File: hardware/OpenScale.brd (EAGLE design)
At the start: 54.6 x 40.6 mm, 58 parts, among them U1 HX711, U3 TMP102, U4 ATMEGA328P_TQFP, U5 MIC52055-5V, U6 FT231X, Y2 16MHZ

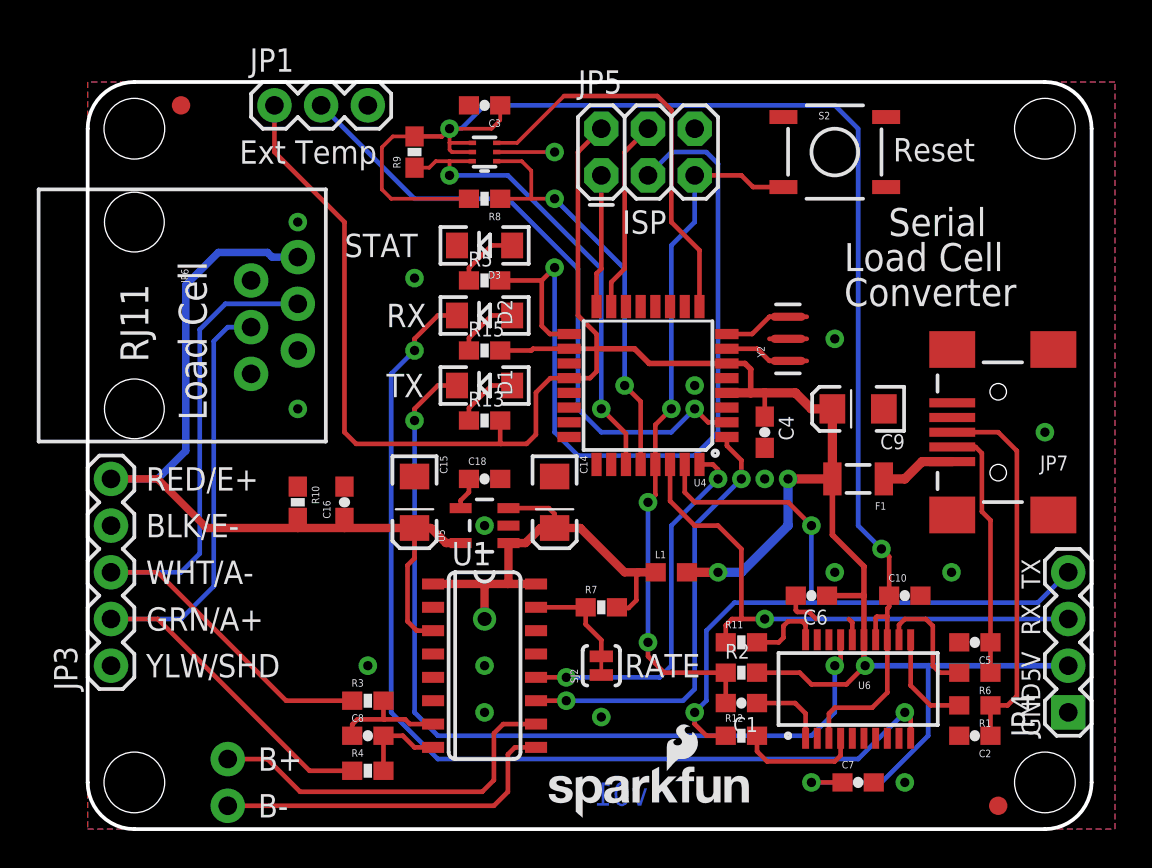
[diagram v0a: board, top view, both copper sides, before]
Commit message: Lots of changes. v02 ready for proto.
Changed to RJ45, FTDI connection, MOSFETs to temp sensor, silk, shutdown
from temp sensor to ATmega.
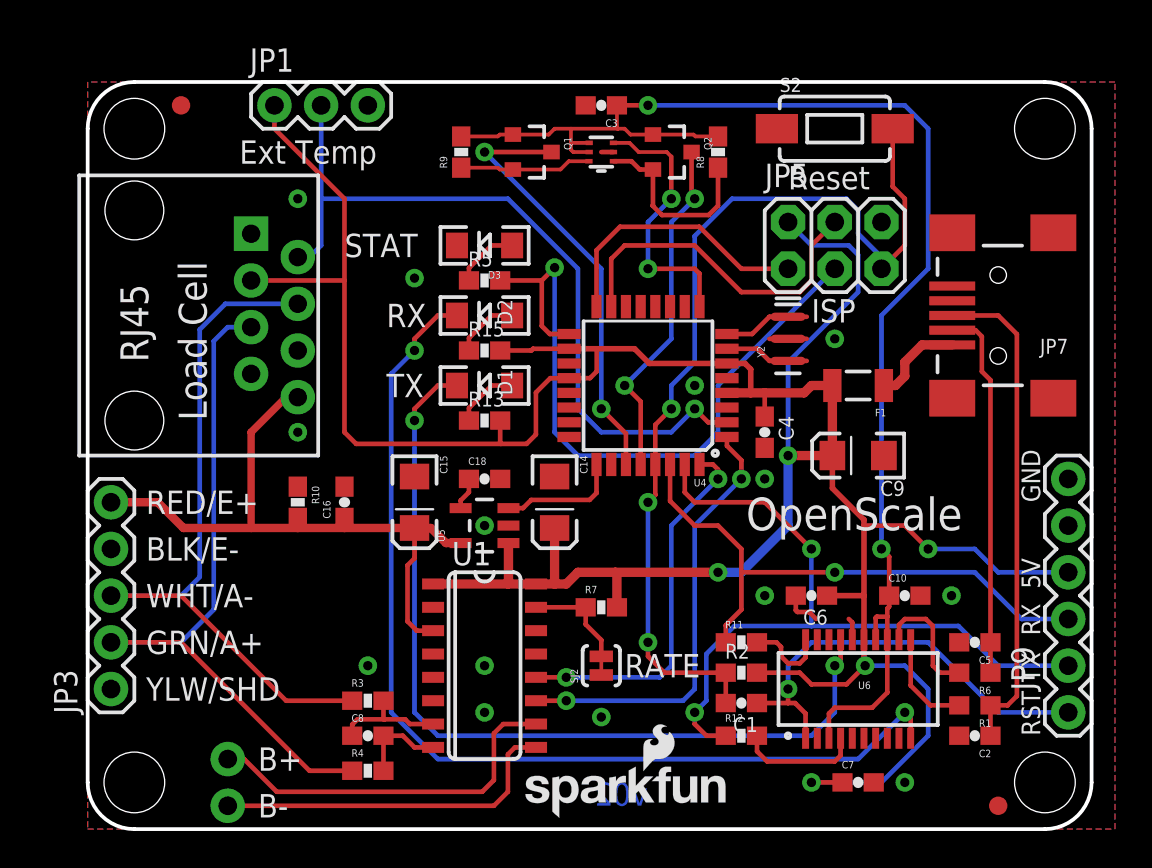
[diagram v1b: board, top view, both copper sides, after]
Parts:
- removed JP4: (no value), SparkFun-Connectors:1X04
- removed L1: 30Ohm 1.8A, SparkFun-Passives:0603
- added JP9: FTDI_BASIC, SparkFun-Connectors:FTDI_BASIC
- added Q1, Q2: 200mA/50V, SparkFun-DiscreteSemi:SOT23-3
- JP6: value RJ11 -> RJ45; device SparkFun-Connectors:RJ11-6 -> SparkFun-Connectors:RJ45-8
- R5: value 330 -> 1K
- S2: device SparkFun-Electromechanical:TACTILE-SWITCH-SMD -> SparkFun-Electromechanical:TACTILE-SWITCH-1101NE
- moved R8 13.0 mm to (34.3, 36.8), turned to 90 degrees
- moved JP5 11.4 mm to (38.1, 30.5)
- moved C3 6.35 mm to (27.9, 39.4)
- moved JP7 6.35 mm to (49.5, 27.9)
- moved U3 6.35 mm to (27.9, 36.8)
- moved F1 5.08 mm to (41.9, 24.1)
- moved C9 2.54 mm to (41.9, 20.3)
- moved R9 2.54 mm to (20.3, 36.8)
- moved LOGO1 1.27 mm to (23.4, 0.51)
- moved S2 1.27 mm to (40.6, 38.1)
- moved JP3 1.27 mm to (1.27, 7.62)
- moved LOGO4 0.89 mm to (33.1, 17.8)
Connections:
- removed net VCC: C14.A, L1.1, R7.2, U1.1, U1.16, U5.1, U5.3
- new net AMP_EN: U4.25, U5.3
- new net LV_SCL: Q2.2, R8.1, U3.1
- new net LV_SDA: Q1.2, R9.1, U3.6
- net 3.3V: now also Q1.1, Q2.1
- net 5V: now also C14.A, JP6.3, JP9.VCC, R7.2, U1.1, U1.16, U5.1; no longer JP4.2, L1.2
- net A+: now also JP6.5; no longer JP6.4
- net A-: now also JP6.4; no longer JP6.3
- net AVDD: now also JP6.8; no longer JP6.1
- net DTR: now also JP9.DTR
- net GND: now also JP6.1, JP6.6, JP6.7, JP9.GND; no longer JP4.1, JP6.2, JP6.5
- net RST: now also S2.2; no longer S2.3
- net RXD: now also JP9.TXO; no longer JP4.3
- net SCL: now also Q2.3; no longer R8.1, U3.1
- net SDA: now also Q1.3; no longer R9.1, U3.6
- net TEMP_DAT: now also JP6.2
- net TXD: now also JP9.RXI; no longer JP4.4
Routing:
- net 5V: track 133.4 -> 170.1 mm, vias 4 -> 5
- net VCC: track 25.3 -> 0.00 mm, vias 1 -> 0
- net DTR: track 4.23 -> 23.6 mm, vias 0 -> 1
- net RST: track 38.6 -> 52.3 mm
- net AVDD: track 49.1 -> 36.4 mm
- net LV_SCL: track 0.00 -> 10.4 mm
- net D11: track 10.5 -> 18.8 mm
- net D12: track 7.25 -> 15.0 mm
- net D13: track 45.5 -> 37.8 mm
- net ALERT: track 22.2 -> 14.8 mm, vias 0 -> 2
- net LV_SDA: track 0.00 -> 7.18 mm
- net TEMP_DAT: track 34.7 -> 41.8 mm
- net AMP_EN: track 0.00 -> 6.69 mm
- net N$7: track 20.6 -> 26.9 mm
- net N$4: track 13.9 -> 20.2 mm
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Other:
- board text added: "BLK"
- board text added: "FTDI"
- board text added: "GRN"
- board text added: "OpenScale"
- board text added: "RJ45"
- board text added: "RST"
- board text removed: "Converter"
- board text removed: "RJ11"
- board text removed: "Serial"

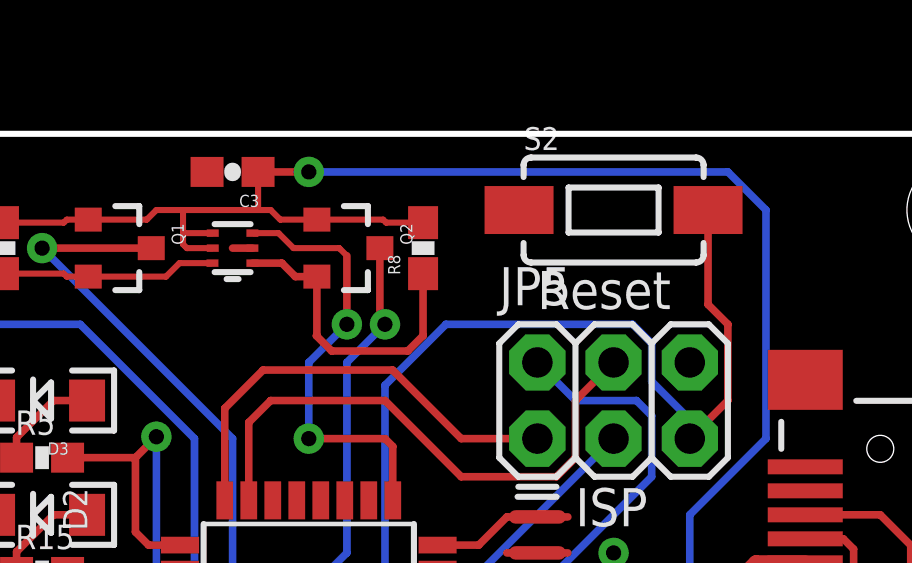
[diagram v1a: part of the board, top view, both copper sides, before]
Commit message: Silk fix. Dim fix. Reroute traces to TMP102.
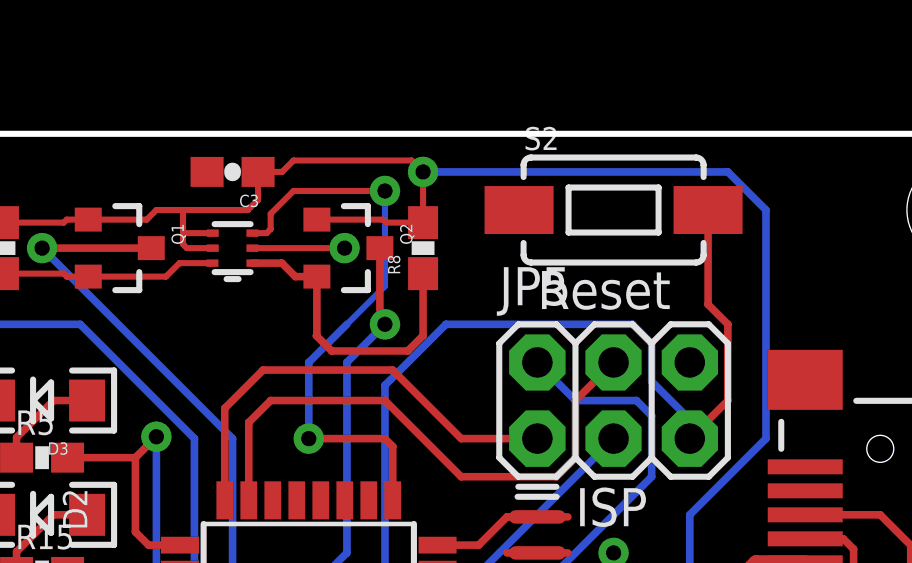
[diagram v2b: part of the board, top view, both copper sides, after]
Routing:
- net ALERT: track 14.8 -> 19.3 mm
- net GND: track 3.97 -> 6.38 mm, vias 14 -> 15
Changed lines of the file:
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@@
 <layer number="39" name="tKeepout" color="4" fill="11" visible="no" active="yes"/>
 <layer number="40" name="bKeepout" color="1" fill="11" visible="no" active="yes"/>
-<layer number="41" name="tRestrict" color="4" fill="10" visible="no" active="yes"/>
+<layer number="41" name="tRestrict" color="4" fill="10" visible="yes" active="yes"/>
 <layer number="42" name="bRestrict" color="1" fill="10" visible="no" active="yes"/>
 <layer number="43" name="vRestrict" color="2" fill="10" visible="no" active="yes"/>
@@
 <text x="3.175" y="17.145" size="1.27" layer="21" font="vector" ratio="15">RED/E+</text>
 <text x="35.56" y="15.113" size="2.032" layer="22" font="vector" ratio="15" rot="MR0">OpenScale</text>
-<text x="15.24" y="30.48" size="1.27" layer="22" font="vector" ratio="15" rot="MR0">E+</text>
-<text x="15.24" y="27.94" size="1.27" layer="22" font="vector" ratio="15" rot="MR0">A-</text>
-<text x="16.129" y="25.4" size="1.27" layer="22" font="vector" ratio="15" rot="MR0">SHD</text>
-<text x="7.0485" y="24.1935" size="1.27" layer="22" font="vector" ratio="15" rot="MR0">B+</text>
+<text x="12.7" y="24.13" size="1.27" layer="22" font="vector" ratio="15" rot="MR180">E+</text>
+<text x="12.7" y="29.21" size="1.27" layer="22" font="vector" ratio="15" rot="MR180">A-</text>
+<text x="12.7" y="26.67" size="1.27" layer="22" font="vector" ratio="15" rot="MR180">SHD</text>
 <text x="7.0485" y="26.6065" size="1.27" layer="22" font="vector" ratio="15" rot="MR0">A+</text>
-<text x="7.0485" y="29.1465" size="1.27" layer="22" font="vector" ratio="15" rot="MR0">E-</text>
+<text x="7.0485" y="24.0665" size="1.27" layer="22" font="vector" ratio="15" rot="MR0">E-</text>
 <text x="3.302" y="25.4" size="1.524" layer="21" font="vector" ratio="15" rot="R90">RJ45</text>
 <text x="6.477" y="22.225" size="1.524" layer="21" font="vector" ratio="15" rot="R90">Load Cell</text>
@@
 <dimension x1="0" y1="40.64" x2="54.61" y2="40.64" x3="27.305" y3="57.15" textsize="1.778" textratio="15" layer="47" unit="inch"/>
 <dimension x1="2.54" y1="38.1" x2="52.07" y2="38.1" x3="27.305" y3="50.8" textsize="1.778" textratio="15" layer="47" unit="inch"/>
-<dimension x1="49.53" y1="21.59" x2="49.53" y2="40.64" x3="67.31" y3="31.115" textsize="1.778" textratio="15" layer="47" unit="inch"/>
+<dimension x1="49.53" y1="27.94" x2="49.53" y2="40.64" x3="67.31" y3="34.29" textsize="1.778" textratio="15" layer="47" unit="inch"/>
 <dimension x1="53.34" y1="6.35" x2="53.34" y2="0" x3="67.31" y3="3.175" textsize="1.778" textratio="15" layer="47" unit="inch"/>
-<dimension x1="1.27" y1="8.89" x2="1.27" y2="0" x3="-3.81" y3="4.445" textsize="1.778" textratio="15" layer="47" unit="inch"/>
+<dimension x1="1.27" y1="7.62" x2="1.27" y2="0" x3="-3.81" y3="3.81" textsize="1.778" textratio="15" layer="47" unit="inch"/>
 <dimension x1="0" y1="40.64" x2="0" y2="27.94" x3="-20.32" y3="34.29" textsize="1.778" textratio="15" layer="47" unit="inch"/>
-<dimension x1="-5.588" y1="34.798" x2="0" y2="34.798" x3="-2.794" y3="43.18" textsize="1.778" textratio="15" layer="47" unit="inch"/>
+<dimension x1="-8.255" y1="34.798" x2="0" y2="34.798" x3="-4.1275" y3="43.18" textsize="1.778" textratio="15" layer="47" unit="inch"/>
 <dimension x1="7.62" y1="1.27" x2="0" y2="1.27" x3="3.81" y3="-3.81" textsize="1.778" textratio="15" layer="47" unit="inch"/>
 <text x="9.271" y="3.175" size="1.27" layer="21" font="vector" ratio="15">B+</text>
@@
 <text x="49.53" y="17.78" size="1.016" layer="22" font="vector" ratio="15" rot="MR90">BLK</text>
 <text x="49.53" y="5.08" size="1.016" layer="22" font="vector" ratio="15" rot="MR90">GRN</text>
+<text x="7.0485" y="29.1465" size="1.27" layer="22" font="vector" ratio="15" rot="MR0">5V</text>
+<text x="12.573" y="31.75" size="1.27" layer="22" font="vector" ratio="15" rot="MR180">SIG</text>
+<rectangle x1="27.559" y1="35.941" x2="28.321" y2="37.719" layer="41"/>
 </plain>
 <attributes>
@@
 <contactref element="JP6" pad="1"/>
 <contactref element="JP9" pad="GND"/>
-<wire x1="28.6" y1="36.83" x2="27.94" y2="36.83" width="0.254" layer="1"/>
+<wire x1="28.6" y1="36.83" x2="31.6738" y2="36.83" width="0.2032" layer="1"/>
+<via x="31.6738" y="36.83" extent="1-16" drill="0.508"/>
 </signal>
 <signal name="RST">
@@
 <wire x1="26.289" y1="36.957" x2="26.289" y2="37.338" width="0.2032" layer="1"/>
 <wire x1="26.289" y1="37.338" x2="26.289" y2="38.1" width="0.2032" layer="1"/>
-<wire x1="28.79" y1="39.37" x2="28.79" y2="38.139" width="0.2032" layer="1"/>
-<wire x1="26.289" y1="38.1" x2="28.829" y2="38.1" width="0.2032" layer="1"/>
 <wire x1="26.416" y1="36.83" x2="26.289" y2="36.957" width="0.2032" layer="1"/>
 <wire x1="27.28" y1="37.33" x2="26.297" y2="37.33" width="0.2032" layer="1"/>
@@
 <contactref element="Q1" pad="1"/>
 <contactref element="Q2" pad="1"/>
-<wire x1="30.75" y1="37.78" x2="29.53" y2="37.78" width="0.2032" layer="1"/>
-<wire x1="29.53" y1="37.78" x2="29.21" y2="38.1" width="0.2032" layer="1"/>
-<wire x1="29.21" y1="38.1" x2="28.829" y2="38.1" width="0.2032" layer="1"/>
-<wire x1="28.79" y1="38.139" x2="28.829" y2="38.1" width="0.2032" layer="1"/>
 <wire x1="23.13" y1="37.78" x2="22.413" y2="37.78" width="0.2032" layer="1"/>
 <wire x1="22.413" y1="37.78" x2="22.313" y2="37.68" width="0.2032" layer="1"/>
@@
 <wire x1="25.08" y1="37.78" x2="25.4" y2="38.1" width="0.2032" layer="1"/>
 <wire x1="25.4" y1="38.1" x2="26.289" y2="38.1" width="0.2032" layer="1"/>
-<via x="30.48" y="39.37" extent="1-16" drill="0.508"/>
-<wire x1="30.48" y1="39.37" x2="28.79" y2="39.37" width="0.254" layer="1"/>
+<via x="34.29" y="39.37" extent="1-16" drill="0.508"/>
 <wire x1="43.18" y1="15.24" x2="43.18" y2="27.94" width="0.254" layer="16"/>
 <wire x1="43.18" y1="27.94" x2="45.72" y2="30.48" width="0.254" layer="16"/>
 <wire x1="45.72" y1="30.48" x2="45.72" y2="38.1" width="0.254" layer="16"/>
-<wire x1="30.48" y1="39.37" x2="44.45" y2="39.37" width="0.254" layer="16"/>
+<wire x1="34.29" y1="39.37" x2="44.45" y2="39.37" width="0.254" layer="16"/>
 <wire x1="44.45" y1="39.37" x2="45.72" y2="38.1" width="0.254" layer="16"/>
+<wire x1="26.289" y1="38.1" x2="28.448" y2="38.1" width="0.2032" layer="1"/>
+<wire x1="28.79" y1="39.37" x2="28.79" y2="38.442" width="0.2032" layer="1"/>
+<wire x1="28.79" y1="38.442" x2="28.448" y2="38.1" width="0.2032" layer="1"/>
+<wire x1="34.29" y1="37.68" x2="34.29" y2="39.37" width="0.2032" layer="1"/>
+<wire x1="28.79" y1="39.37" x2="29.591" y2="39.37" width="0.2032" layer="1"/>
+<wire x1="29.591" y1="39.37" x2="29.972" y2="39.751" width="0.2032" layer="1"/>
+<wire x1="29.972" y1="39.751" x2="33.909" y2="39.751" width="0.2032" layer="1"/>
+<wire x1="33.909" y1="39.751" x2="34.29" y2="39.37" width="0.2032" layer="1"/>
 </signal>
 <signal name="RXLED">
@@
 <contactref element="U3" pad="3"/>
 <contactref element="U4" pad="9"/>
-<wire x1="28.6" y1="37.33" x2="29.472" y2="37.33" width="0.2032" layer="1"/>
-<wire x1="29.472" y1="37.33" x2="29.972" y2="36.83" width="0.2032" layer="1"/>
-<wire x1="29.972" y1="36.83" x2="31.496" y2="36.83" width="0.2032" layer="1"/>
-<wire x1="31.496" y1="36.83" x2="31.75" y2="36.576" width="0.2032" layer="1"/>
 <wire x1="33.28" y1="28.4226" x2="33.28" y2="30.22" width="0.254" layer="1"/>
 <wire x1="33.28" y1="30.22" x2="33.02" y2="30.48" width="0.254" layer="1"/>
@@
 <wire x1="30.48" y1="30.48" x2="30.48" y2="33.02" width="0.254" layer="16"/>
 <wire x1="30.48" y1="33.02" x2="31.75" y2="34.29" width="0.254" layer="16"/>
-<via x="31.75" y="34.29" extent="1-16" drill="0.508"/>
-<wire x1="31.75" y1="34.29" x2="31.75" y2="36.576" width="0.254" layer="1"/>
+<wire x1="28.6" y1="37.33" x2="29.075" y2="37.33" width="0.2032" layer="1"/>
+<wire x1="29.075" y1="37.33" x2="29.21" y2="37.465" width="0.2032" layer="1"/>
+<wire x1="29.21" y1="37.465" x2="29.21" y2="37.973" width="0.2032" layer="1"/>
+<wire x1="29.21" y1="37.973" x2="29.972" y2="38.735" width="0.2032" layer="1"/>
+<wire x1="29.972" y1="38.735" x2="33.02" y2="38.735" width="0.2032" layer="1"/>
+<via x="33.02" y="38.735" extent="1-16" drill="0.508"/>
+<wire x1="31.75" y1="34.29" x2="33.02" y2="35.56" width="0.2032" layer="16"/>
+<wire x1="33.02" y1="35.56" x2="33.02" y2="38.735" width="0.2032" layer="16"/>
 </signal>
 <signal name="D13">

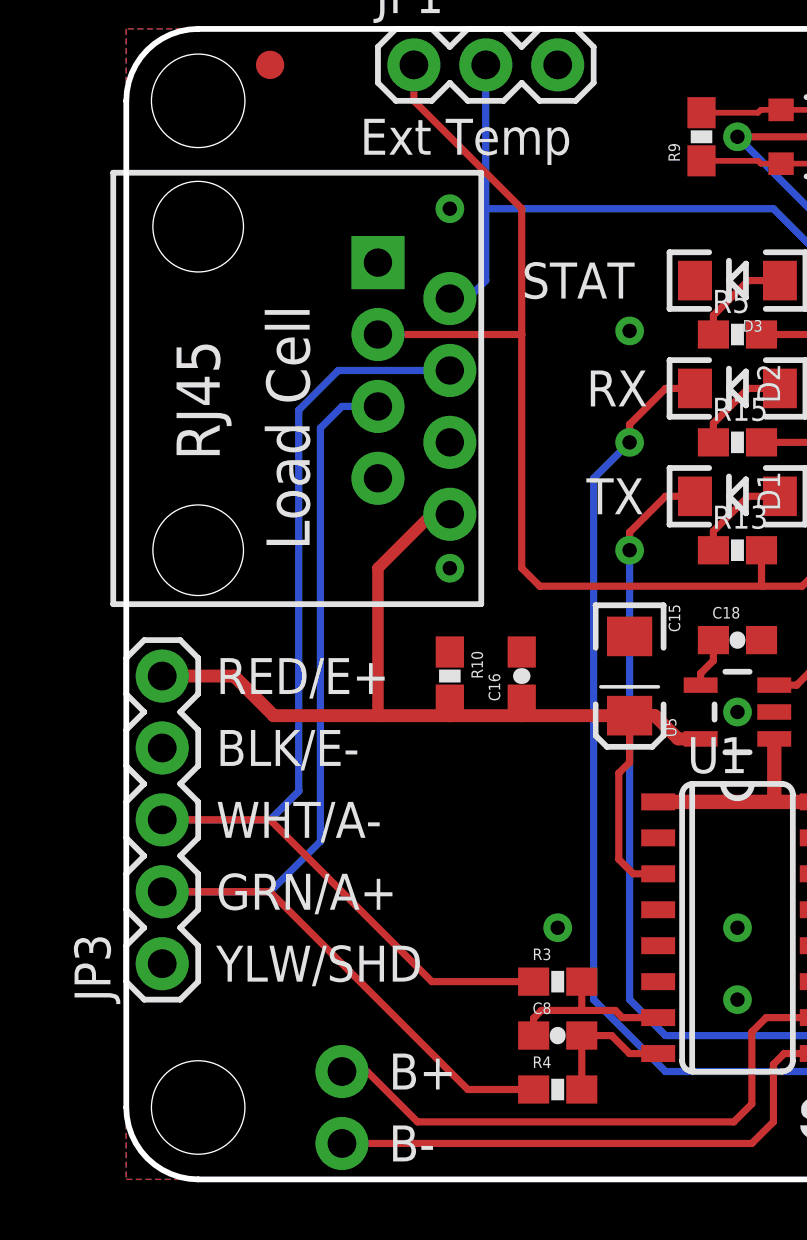
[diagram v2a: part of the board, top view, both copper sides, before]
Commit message: Bumped RJ45 to fix issue #3
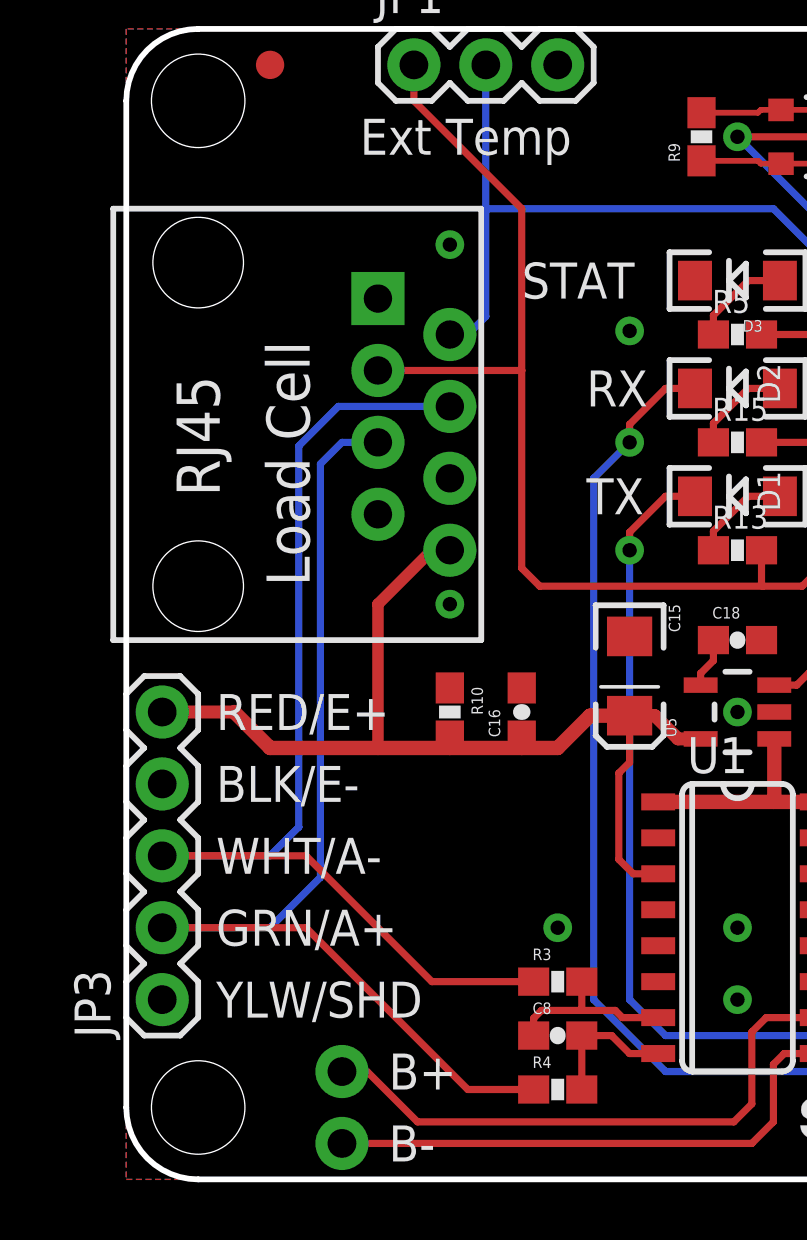
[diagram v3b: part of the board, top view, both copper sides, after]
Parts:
- moved JP3 1.27 mm to (1.27, 6.35)
- moved C16 1.27 mm to (14.0, 16.5)
- moved JP6 1.27 mm to (2.54, 26.7)
- moved R10 1.27 mm to (11.4, 16.5)
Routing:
- net TEMP_DAT: track 41.8 -> 43.0 mm
- net A-: track 40.1 -> 39.6 mm
- net A+: track 39.3 -> 38.8 mm
